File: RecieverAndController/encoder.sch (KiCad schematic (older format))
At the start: 8 parts

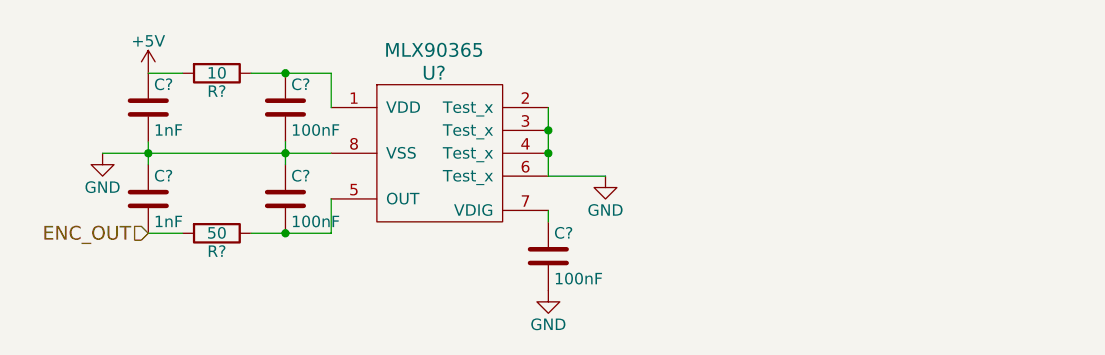
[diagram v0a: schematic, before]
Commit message: adding footprints to schematic
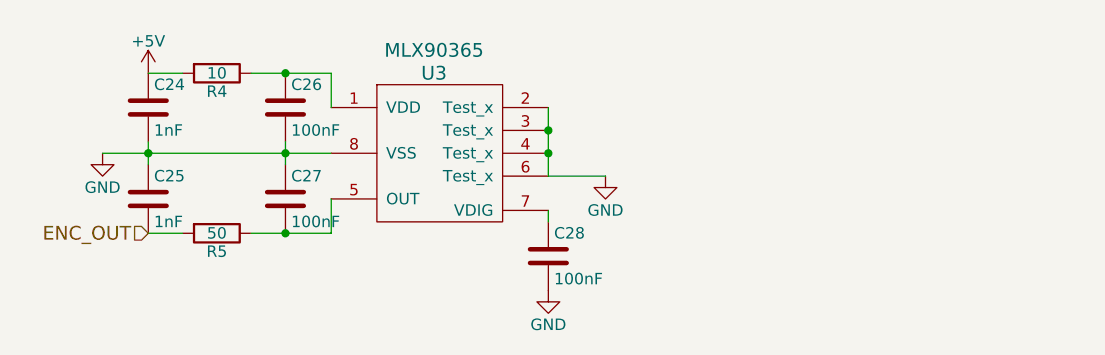
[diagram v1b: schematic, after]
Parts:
- C24, C25, C26, C27, C28: renamed from C?; footprint (none) -> Capacitors_SMD:C_0603
- R4, R5: renamed from R?; footprint (none) -> Resistors_SMD:R_0603
- U3: renamed from U?; footprint (none) -> Housings_SOIC:SOIC-8_3.9x4.9mm_Pitch1.27mm
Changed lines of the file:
@@
 $EndDescr
 $Comp
-L MLX90365 U?
+L MLX90365 U3
 U 1 1 5A9ADA9B
 P 3250 3050
-F 0 "U?" H 3250 3350 60  0000 C CNN
+F 0 "U3" H 3250 3350 60  0000 C CNN
 F 1 "MLX90365" H 3250 3450 60  0000 C CNN
-F 2 "" H 3250 3050 60  0001 C CNN
+F 2 "Housings_SOIC:SOIC-8_3.9x4.9mm_Pitch1.27mm" H 3250 3050 60  0001 C CNN
 F 3 "" H 3250 3050 60  0001 C CNN
 	1    3250 3050
@@
 $EndComp
 $Comp
-L R R?
+L R R4
 U 1 1 5A9ADC47
 P 2300 2750
-F 0 "R?" V 2380 2750 50  0000 C CNN
+F 0 "R4" V 2380 2750 50  0000 C CNN
 F 1 "10" V 2300 2750 50  0000 C CNN
-F 2 "" V 2230 2750 50  0001 C CNN
+F 2 "Resistors_SMD:R_0603" V 2230 2750 50  0001 C CNN
 F 3 "" H 2300 2750 50  0001 C CNN
 	1    2300 2750
@@
 $EndComp
 $Comp
-L C C?
+L C C26
 U 1 1 5A9ADC70
 P 2600 2900
-F 0 "C?" H 2625 3000 50  0000 L CNN
+F 0 "C26" H 2625 3000 50  0000 L CNN
 F 1 "100nF" H 2625 2800 50  0000 L CNN
-F 2 "" H 2638 2750 50  0001 C CNN
+F 2 "Capacitors_SMD:C_0603" H 2638 2750 50  0001 C CNN
 F 3 "" H 2600 2900 50  0001 C CNN
 	1    2600 2900
@@
 $EndComp
 $Comp
-L C C?
+L C C27
 U 1 1 5A9ADC92
 P 2600 3300
-F 0 "C?" H 2625 3400 50  0000 L CNN
+F 0 "C27" H 2625 3400 50  0000 L CNN
 F 1 "100nF" H 2625 3200 50  0000 L CNN
-F 2 "" H 2638 3150 50  0001 C CNN
+F 2 "Capacitors_SMD:C_0603" H 2638 3150 50  0001 C CNN
 F 3 "" H 2600 3300 50  0001 C CNN
 	1    2600 3300
@@
 $EndComp
 $Comp
-L R R?
+L R R5
 U 1 1 5A9ADD10
 P 2300 3450
-F 0 "R?" V 2380 3450 50  0000 C CNN
+F 0 "R5" V 2380 3450 50  0000 C CNN
 F 1 "50" V 2300 3450 50  0000 C CNN
-F 2 "" V 2230 3450 50  0001 C CNN
+F 2 "Resistors_SMD:R_0603" V 2230 3450 50  0001 C CNN
 F 3 "" H 2300 3450 50  0001 C CNN
 	1    2300 3450
@@
 $EndComp
 $Comp
-L C C?
+L C C25
 U 1 1 5A9ADD4B
 P 2000 3300
-F 0 "C?" H 2025 3400 50  0000 L CNN
+F 0 "C25" H 2025 3400 50  0000 L CNN
 F 1 "1nF" H 2025 3200 50  0000 L CNN
-F 2 "" H 2038 3150 50  0001 C CNN
+F 2 "Capacitors_SMD:C_0603" H 2038 3150 50  0001 C CNN
 F 3 "" H 2000 3300 50  0001 C CNN
 	1    2000 3300
@@
 $EndComp
 $Comp
-L C C?
+L C C24
 U 1 1 5A9ADD85
 P 2000 2900
-F 0 "C?" H 2025 3000 50  0000 L CNN
+F 0 "C24" H 2025 3000 50  0000 L CNN
 F 1 "1nF" H 2025 2800 50  0000 L CNN
-F 2 "" H 2038 2750 50  0001 C CNN
+F 2 "Capacitors_SMD:C_0603" H 2038 2750 50  0001 C CNN
 F 3 "" H 2000 2900 50  0001 C CNN
 	1    2000 2900
@@
 $EndComp
 $Comp
-L GND #PWR?
+L GND #PWR031
 U 1 1 5A9ADF2A
 P 1800 3100
-F 0 "#PWR?" H 1800 2850 50  0001 C CNN
+F 0 "#PWR031" H 1800 2850 50  0001 C CNN
 F 1 "GND" H 1800 2950 50  0000 C CNN
 F 2 "" H 1800 3100 50  0001 C CNN
@@
 $EndComp
 $Comp
-L +5V #PWR?
+L +5V #PWR032
 U 1 1 5A9AE4C6
 P 2000 2750
-F 0 "#PWR?" H 2000 2600 50  0001 C CNN
+F 0 "#PWR032" H 2000 2600 50  0001 C CNN
 F 1 "+5V" H 2000 2890 50  0000 C CNN
 F 2 "" H 2000 2750 50  0001 C CNN
@@
 ENC_OUT
 $Comp
-L GND #PWR?
+L GND #PWR033
 U 1 1 5A9AEA7E
 P 4000 3200
-F 0 "#PWR?" H 4000 2950 50  0001 C CNN
+F 0 "#PWR033" H 4000 2950 50  0001 C CNN
 F 1 "GND" H 4000 3050 50  0000 C CNN
 F 2 "" H 4000 3200 50  0001 C CNN
@@
 	3750 3200 4000 3200
 $Comp
-L C C?
+L C C28
 U 1 1 5A9AEC0C
 P 3750 3550
-F 0 "C?" H 3775 3650 50  0000 L CNN
+F 0 "C28" H 3775 3650 50  0000 L CNN
 F 1 "100nF" H 3775 3450 50  0000 L CNN
-F 2 "" H 3788 3400 50  0001 C CNN
+F 2 "Capacitors_SMD:C_0603" H 3788 3400 50  0001 C CNN
 F 3 "" H 3750 3550 50  0001 C CNN
 	1    3750 3550
@@
 	3750 3350 3750 3400
 $Comp
-L GND #PWR?
+L GND #PWR034
 U 1 1 5A9AEC74
 P 3750 3700
-F 0 "#PWR?" H 3750 3450 50  0001 C CNN
+F 0 "#PWR034" H 3750 3450 50  0001 C CNN
 F 1 "GND" H 3750 3550 50  0000 C CNN
 F 2 "" H 3750 3700 50  0001 C CNN

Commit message: adding start of pcb
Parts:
- added J? (x2): Conn_01x03, symbol Conn_01x03
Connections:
- net +5V: now also J?.1 (Pin_1); no longer C24.1, R4.2
- net ENC_OUT: now also J?.2 (Pin_2); no longer C25.2, R5.2
- net GND: now also J?.3 (Pin_3); no longer C24.2, C25.1, C26.2, C27.1, C28.2, U3.2 (Test_x), U3.3 (Test_x), U3.4 (Test_x), U3.6 (Test_x), U3.8 (VSS)
- new net 5V_L: C24.1, J?.1 (Pin_1), R4.2
- new net ENC_OUT_L: C25.2, J?.2 (Pin_2), R5.2
- new net GND_L: C24.2, C25.1, C26.2, C27.1, C28.2, J?.3 (Pin_3), U3.2 (Test_x), U3.3 (Test_x), U3.4 (Test_x), U3.6 (Test_x), U3.8 (VSS)
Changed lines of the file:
@@
-$EndComp
-$Comp
-L C C25
-U 1 1 5A9ADD4B
-P 2000 3300
-F 0 "C25" H 2025 3400 50  0000 L CNN
-F 1 "1nF" H 2025 3200 50  0000 L CNN
-F 2 "Capacitors_SMD:C_0603" H 2038 3150 50  0001 C CNN
-F 3 "" H 2000 3300 50  0001 C CNN
-	1    2000 3300
-	1    0    0    -1
 $EndComp
 $Comp
@@
 F 3 "" H 2000 2900 50  0001 C CNN
 	1    2000 2900
-	1    0    0    -1
-$EndComp
-$Comp
-L GND #PWR031
-U 1 1 5A9ADF2A
-P 1800 3100
-F 0 "#PWR031" H 1800 2850 50  0001 C CNN
-F 1 "GND" H 1800 2950 50  0000 C CNN
-F 2 "" H 1800 3100 50  0001 C CNN
-F 3 "" H 1800 3100 50  0001 C CNN
-	1    1800 3100
-	1    0    0    -1
-$EndComp
-$Comp
-L +5V #PWR032
-U 1 1 5A9AE4C6
-P 2000 2750
-F 0 "#PWR032" H 2000 2600 50  0001 C CNN
-F 1 "+5V" H 2000 2890 50  0000 C CNN
-F 2 "" H 2000 2750 50  0001 C CNN
-F 3 "" H 2000 2750 50  0001 C CNN
-	1    2000 2750
-	1    0    0    -1
-$EndComp
-Text HLabel 2000 3450 0    60   Input ~ 0
-ENC_OUT
-$Comp
-L GND #PWR033
-U 1 1 5A9AEA7E
-P 4000 3200
-F 0 "#PWR033" H 4000 2950 50  0001 C CNN
-F 1 "GND" H 4000 3050 50  0000 C CNN
-F 2 "" H 4000 3200 50  0001 C CNN
-F 3 "" H 4000 3200 50  0001 C CNN
-	1    4000 3200
 	1    0    0    -1
 $EndComp
@@
 	3750 3350 3750 3400
 $Comp
-L GND #PWR034
-U 1 1 5A9AEC74
-P 3750 3700
-F 0 "#PWR034" H 3750 3450 50  0001 C CNN
-F 1 "GND" H 3750 3550 50  0000 C CNN
-F 2 "" H 3750 3700 50  0001 C CNN
-F 3 "" H 3750 3700 50  0001 C CNN
-	1    3750 3700
+L Conn_01x03 J?
+U 1 1 5ACAF373
+P 4650 2800
+F 0 "J?" H 4650 3000 50  0000 C CNN
+F 1 "Conn_01x03" H 4650 2600 50  0000 C CNN
+F 2 "" H 4650 2800 50  0001 C CNN
+F 3 "" H 4650 2800 50  0001 C CNN
+	1    4650 2800
 	1    0    0    -1
 $EndComp
+Text Label 4450 2900 2    60   ~ 0
+GND_L
+Text Label 4450 2800 2    60   ~ 0
+ENC_OUT_L
+Text Label 4450 2700 2    60   ~ 0
+5V_L
+Text Label 2000 2750 2    60   ~ 0
+5V_L
+$Comp
+L C C25
+U 1 1 5A9ADD4B
+P 2000 3300
+F 0 "C25" H 2025 3400 50  0000 L CNN
+F 1 "1nF" H 2025 3200 50  0000 L CNN
+F 2 "Capacitors_SMD:C_0603" H 2038 3150 50  0001 C CNN
+F 3 "" H 2000 3300 50  0001 C CNN
+	1    2000 3300
+	1    0    0    -1
+$EndComp
+Text Label 1800 3100 2    60   ~ 0
+GND_L
+Text Label 4000 3200 3    60   ~ 0
+GND_L
+Text Label 3750 3700 2    60   ~ 0
+GND_L
+Text Label 2000 3450 2    60   ~ 0
+ENC_OUT_L
+$Comp
+L Conn_01x03 J?
+U 1 1 5ACAF700
+P 5550 2800
+F 0 "J?" H 5550 3000 50  0000 C CNN
+F 1 "Conn_01x03" H 5850 2800 50  0000 C CNN
+F 2 "" H 5550 2800 50  0001 C CNN
+F 3 "" H 5550 2800 50  0001 C CNN
+	1    5550 2800
+	1    0    0    -1
+$EndComp
+Text HLabel 5350 2800 0    60   Input ~ 0
+ENC_OUT
+$Comp
+L GND #PWR?
+U 1 1 5ACAF7BE
+P 5350 2900
+F 0 "#PWR?" H 5350 2650 50  0001 C CNN
+F 1 "GND" H 5350 2750 50  0000 C CNN
+F 2 "" H 5350 2900 50  0001 C CNN
+F 3 "" H 5350 2900 50  0001 C CNN
+	1    5350 2900
+	1    0    0    -1
+$EndComp
+$Comp
+L +5V #PWR?
+U 1 1 5ACAF7E6
+P 5350 2700
+F 0 "#PWR?" H 5350 2550 50  0001 C CNN
+F 1 "+5V" H 5350 2840 50  0000 C CNN
+F 2 "" H 5350 2700 50  0001 C CNN
+F 3 "" H 5350 2700 50  0001 C CNN
+	1    5350 2700
+	1    0    0    -1
+$EndComp
